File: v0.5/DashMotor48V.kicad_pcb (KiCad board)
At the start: 6 copper layers, 72 x 69.7 mm, 115 parts, among them CN3(OUT)1 XT30(2+2)PB-M.G.B, CN3(OUT)2 XT30(2+2)PB-M.G.B, J1 BM07B-SRSS-TB(LF)(SN), J2 BM07B-SRSS-TB(LF)(SN), J3 Conn_01x02_Pin, Q1 FDMT80080DC, Q2 FDMT80080DC, Q3 FDMT80080DC, Q4 FDMT80080DC, Q5 FDMT80080DC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

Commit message: finish first draft
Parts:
- removed TP2: +48V TestPoint, TestPoint:TestPoint_THTPad_D1.5mm_Drill0.7mm
- removed TP_GND1: GND TestPoint, TestPoint:TestPoint_THTPad_D1.5mm_Drill0.7mm
- R3: moved to B.Cu
- moved TP9 67.9 mm to (28.2, -0.72)
- moved TP8 67.4 mm to (27.6, -2.90)
- moved TP7 63.9 mm to (26.5, -4.92)
- moved TP10 63.3 mm to (25.6, -7.00)
- moved TP_GND2 59.5 mm to (-21.8, 13.5)
- moved TP12 50.9 mm to (6.80, -6.17)
- moved TP11 49.2 mm to (11.0, -32.3)
- moved TP13 44.8 mm to (8.82, -32.7)
- moved TP14 43.2 mm to (7.15, -31.2)
- moved TP4 30.4 mm to (-12.5, -22.2)
- moved TP1 27.5 mm to (-10.8, -9.68)
- moved TP5 26.1 mm to (7.80, -26.7)
- moved TP6 26.1 mm to (6.78, -28.6)
- moved R3 22.9 mm to (6.56, -14.1), turned to 180 degrees
- moved TP3 13.1 mm to (21.0, -19.9)
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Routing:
- net GND: track 19.4 -> 124.7 mm, vias 38 -> 101
- net /SPI-NSS-DRV: track 23.0 -> 65.1 mm
- net /SPI-SCK: track 22.3 -> 63.6 mm
- net +3.3V: track 61.5 -> 100.5 mm, vias 5 -> 11
- net /SPI-MISO: track 19.2 -> 56.8 mm
- net /SPI-MOSI: track 16.9 -> 51.5 mm
- net /SCK: track 46.6 -> 57.5 mm
- net Net-(VR1-FB): track 13.4 -> 23.9 mm
- net /CAN_RX: track 15.9 -> 26.2 mm, vias 0 -> 1
- net /MISO: track 44.3 -> 54.2 mm
- net /MOSI: track 44.0 -> 51.1 mm
- net +5V: track 25.1 -> 31.7 mm
- net /CAN_TX: track 19.9 -> 25.7 mm, vias 0 -> 1
- net /CS: track 24.0 -> 26.2 mm
- net Net-(U2-VCP): track 9.50 -> 7.86 mm
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- added copper zone on F.Cu, net +12V
- added copper zone on F.Cu, net +3.3V
- added copper zone on F.Cu, net /GHA
- added copper zone on F.Cu, net /GHB
- added copper zone on F.Cu, net /GHC
- added copper zone on F.Cu, net /GLA
- added copper zone on F.Cu, net /GLB
- added copper zone on F.Cu, net /GLC
- added copper zone on F.Cu, net GND
- added copper zone on F.Cu, net Net-(U2-VCP)
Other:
- board text removed: "3.3V"
- board text removed: "INDIC"

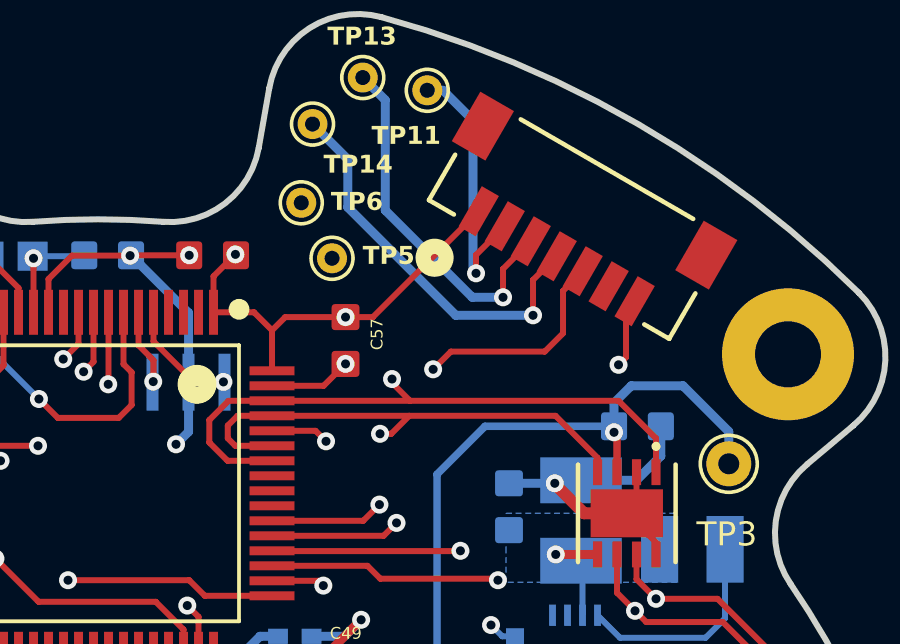
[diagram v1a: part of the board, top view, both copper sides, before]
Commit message: fix canrx tx pin place
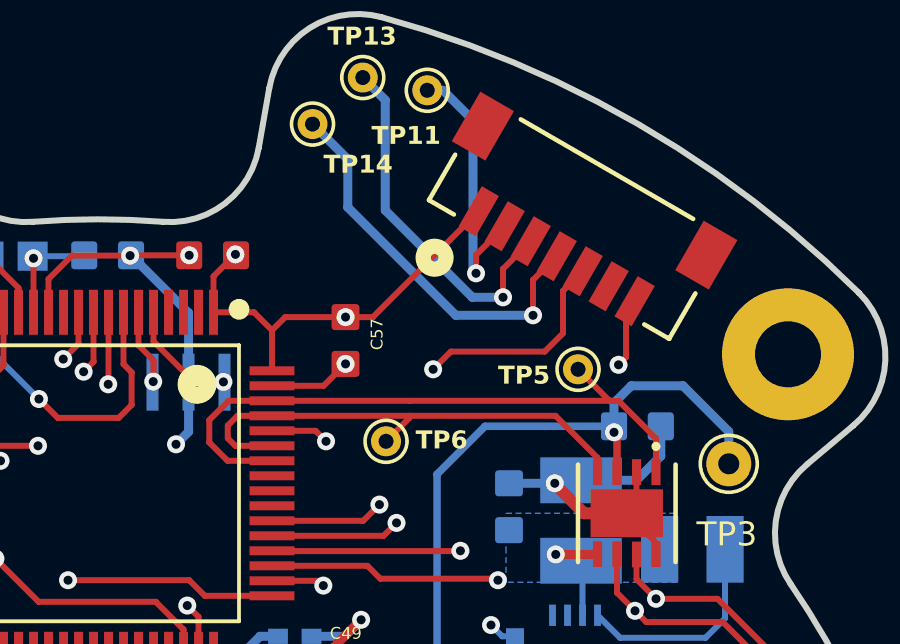
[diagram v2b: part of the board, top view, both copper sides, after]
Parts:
- moved TP5 9.00 mm to (16.0, -23.0)
- moved TP6 8.44 mm to (9.60, -20.6)
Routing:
- net /CAN_RX: track 26.2 -> 17.1 mm, vias 1 -> 0
- net /CAN_TX: track 25.7 -> 21.7 mm, vias 1 -> 0

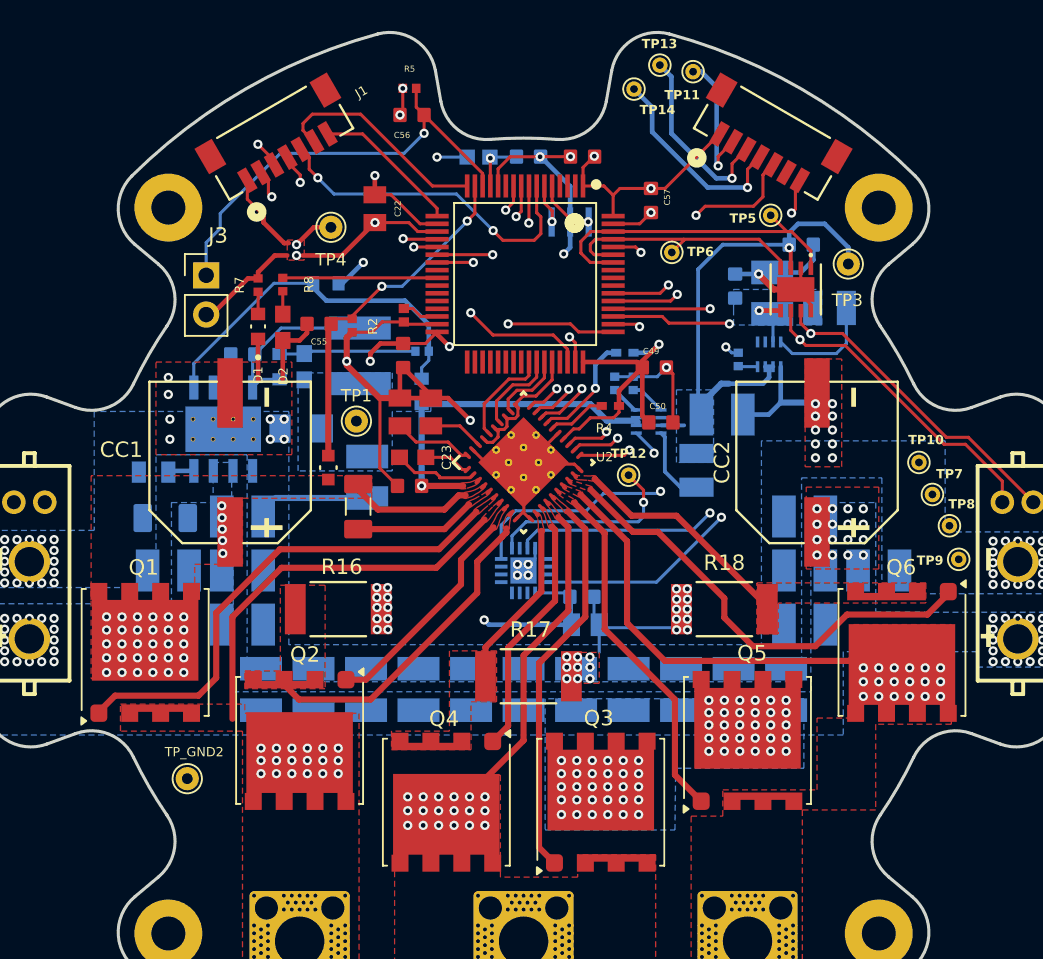
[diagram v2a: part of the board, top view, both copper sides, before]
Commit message: keep tuning few things
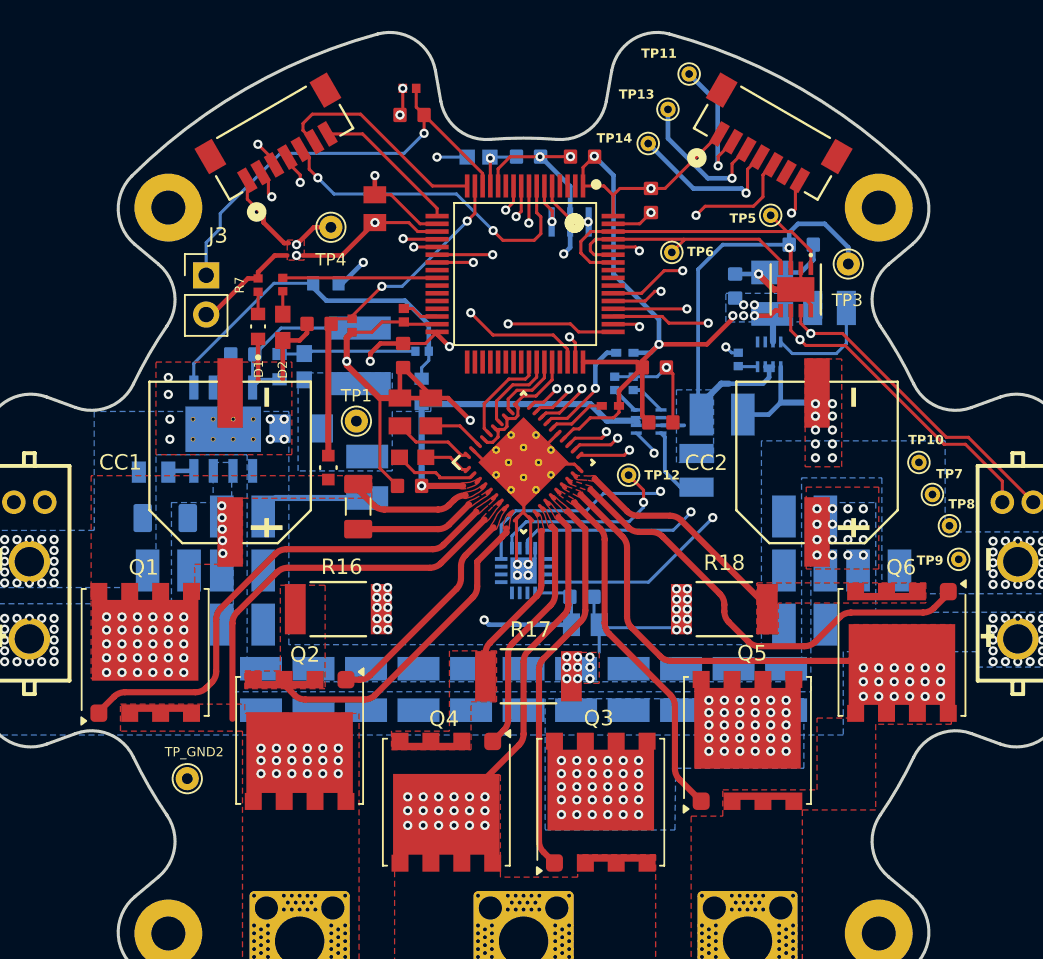
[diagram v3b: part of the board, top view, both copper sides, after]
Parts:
- moved TP14 3.64 mm to (8.07, -27.6)
- moved TP13 2.91 mm to (9.35, -29.9)
- moved TP11 0.30 mm to (10.7, -32.1)
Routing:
- net +3.3V: track 100.5 -> 130.3 mm, vias 11 -> 15
- net /SCK: track 57.5 -> 51.4 mm
- net GND: track 124.7 -> 130.5 mm
- net /MISO: track 54.2 -> 49.2 mm
- net /MOSI: track 51.1 -> 49.8 mm

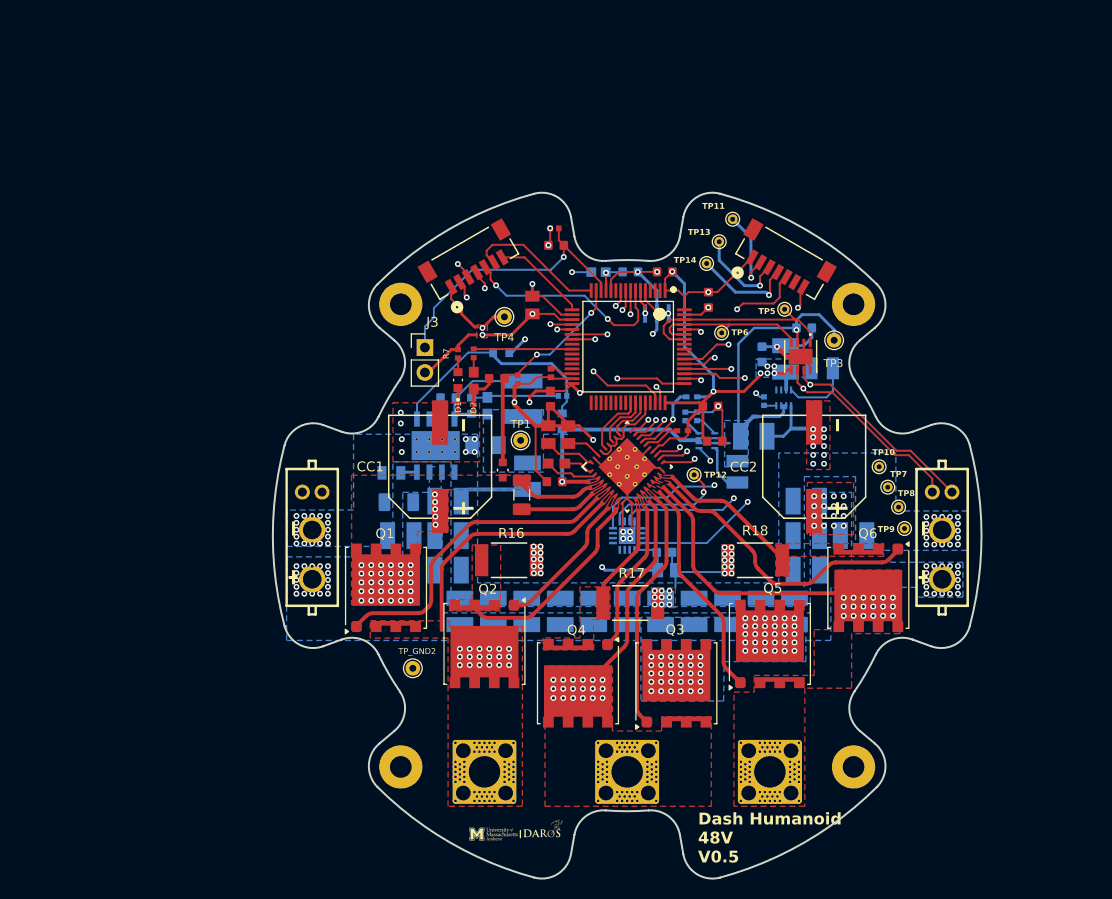
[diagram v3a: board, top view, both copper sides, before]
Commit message: adding more copper to the board
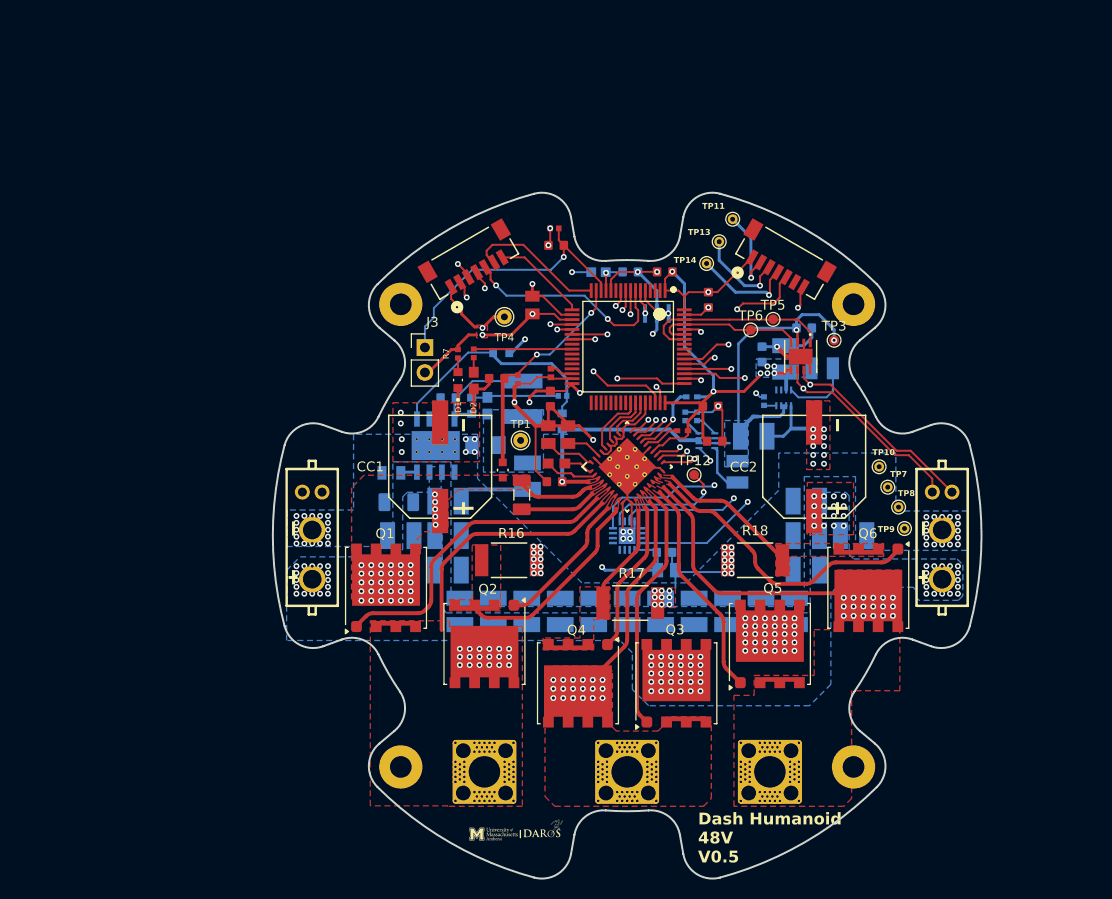
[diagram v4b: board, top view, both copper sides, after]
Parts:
- removed TP_GND2: GND TestPoint, TestPoint:TestPoint_THTPad_D1.5mm_Drill0.7mm
- TP12, TP5, TP6: footprint TestPoint:TestPoint_THTPad_D1.0mm_Drill0.5mm -> TestPoint:TestPoint_Pad_D1.0mm
- TP3: footprint TestPoint:TestPoint_THTPad_D1.5mm_Drill0.7mm -> TestPoint:TestPoint_Pad_D1.0mm
- moved TP6 2.97 mm to (12.6, -20.9)
- moved TP5 1.56 mm to (14.8, -22.0)
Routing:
- net /CAN_TX: track 21.7 -> 20.2 mm
- net /CAN_RX: track 17.1 -> 15.9 mm
- net +5V: vias 1 -> 2

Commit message: keep finishing it
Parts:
- removed TP1: +12V TestPoint, TestPoint:TestPoint_THTPad_D1.5mm_Drill0.7mm
- R14: moved to F.Cu
- TP10, TP7, TP8, TP9: footprint TestPoint:TestPoint_THTPad_D1.0mm_Drill0.5mm -> TestPoint:TestPoint_Pad_D1.0mm
- TP4: footprint TestPoint:TestPoint_THTPad_D1.5mm_Drill0.7mm -> TestPoint:TestPoint_Pad_D1.0mm
- moved TP8 43.9 mm to (-11.8, -22.2)
- moved TP9 43.9 mm to (-9.60, -23.0)
- moved TP10 39.6 mm to (-11.8, -20.0)
- moved TP7 38.7 mm to (-9.60, -18.9)
- moved R6 14.6 mm to (-27.1, -8.43)
- moved R14 4.52 mm to (-10.4, -14.8), turned to 0 degrees
- moved R2 3.08 mm to (-14.2, -15.7)
- moved C40 2.69 mm to (15.6, -10.1)
- moved C42 2.55 mm to (-6.60, -11.7)
- moved L1 2.45 mm to (-10.4, -11.4)
- moved C43 2.40 mm to (-14.1, -10.8)
- moved R9 2.40 mm to (-6.70, -9.20)
- moved C22 2.38 mm to (-10.6, -25.6), turned to 180 degrees
- moved TP4 2.33 mm to (-14.7, -22.9)
- moved L2 2.11 mm to (11.7, -8.55)
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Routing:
- net GND: track 130.5 -> 79.2 mm, vias 101 -> 98
- net /SPI-NSS-DRV: track 65.1 -> 27.3 mm
- net /SPI-SCK: track 63.6 -> 28.4 mm
- net /SPI-MOSI: track 51.5 -> 21.3 mm
- net /SPI-MISO: track 56.8 -> 29.2 mm
- net +3.3V: track 130.3 -> 113.3 mm, vias 15 -> 14
- net /VBAT: track 22.8 -> 31.7 mm, vias 2 -> 4
- net +12V: track 22.7 -> 19.7 mm
- net /CS: track 25.8 -> 22.8 mm
- net +5V: track 31.7 -> 29.0 mm
- net +48V: track 8.13 -> 10.4 mm
- net Net-(VR1-FB): track 23.9 -> 21.7 mm, vias 0 -> 1
- net Net-(U5-SW): track 5.06 -> 3.62 mm
- net /MOSI: track 49.8 -> 48.6 mm
- net /SCK: track 51.4 -> 50.3 mm
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- added copper zone on In3.Cu, net +3.3V
- added copper zone on In3.Cu, net +48V

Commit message: fine tune
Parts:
- C48, R14: moved to B.Cu
- moved R14 13.1 mm to (-23.0, -11.0), turned to 90 degrees
- moved C48 5.28 mm to (-2.75, -15.4), turned to 0 degrees
- moved C51 4.92 mm to (-11.1, -8.70), turned to 90 degrees
- moved R9 2.84 mm to (-4.40, -10.9)
- moved C49 1.81 mm to (9.85, -12.0)
- moved C50 1.36 mm to (9.85, -10.6)
- moved C20 1.30 mm to (-12.0, -4.00)
- moved C26 1.03 mm to (-8.28, -15.7)
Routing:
- net +3.3V: track 113.3 -> 76.7 mm, vias 14 -> 15
- net +12V: track 19.7 -> 8.29 mm
- net GND: track 79.2 -> 76.4 mm, vias 98 -> 114
- net Net-(VR1-FB): track 21.7 -> 23.5 mm, vias 1 -> 0
- net /PHASA: track 25.4 -> 26.8 mm, vias 18 -> 32
- net Net-(U2-VCP): track 7.81 -> 9.16 mm
- net +48V: track 10.4 -> 9.14 mm, vias 143 -> 150
- net /TCK: track 29.4 -> 28.2 mm
- net /MISO: track 48.3 -> 49.1 mm
- net /SPI-MISO: track 29.2 -> 28.5 mm
- net /CAN+: track 77.3 -> 76.7 mm
- net /PHASC: vias 18 -> 32
- net /PHASB: vias 18 -> 32
- added copper zone on B.Cu, net /PHASA
- added copper zone on In2.Cu, net /PHASA
- added copper zone on In3.Cu, net /PHASA
- added copper zone on B.Cu, net /PHASB
- added copper zone on In2.Cu, net /PHASB
- added copper zone on In3.Cu, net /PHASB
- added copper zone on B.Cu, net /PHASC
- added copper zone on In2.Cu, net /PHASC
- added copper zone on In3.Cu, net /PHASC
- added copper zone on In2.Cu, net GND
- added copper zone on In3.Cu, net GND

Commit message: doing fine touch for the routing, almost done
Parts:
- removed TP11: TP_MOSI, TestPoint:TestPoint_THTPad_D1.0mm_Drill0.5mm
- removed TP13: TP_MISO, TestPoint:TestPoint_THTPad_D1.0mm_Drill0.5mm
- removed TP14: TP_SCK, TestPoint:TestPoint_THTPad_D1.0mm_Drill0.5mm
- moved R3 5.40 mm to (1.33, -15.4), turned to 0 degrees
- moved C48 2.00 mm to (-0.91, -16.2), turned to 90 degrees
- moved R11 1.45 mm to (8.55, -12.2)
- moved R10 1.45 mm to (7.35, -12.2)
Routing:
- net +3.3V: track 76.7 -> 64.9 mm
- net /SCK: track 50.3 -> 42.6 mm
- net /MISO: track 49.1 -> 42.0 mm
- net /MOSI: track 48.9 -> 42.2 mm
- net GND: track 76.4 -> 71.5 mm, vias 114 -> 113
- net /SPI-MISO: track 28.5 -> 31.0 mm
- net +12V: track 8.29 -> 7.27 mm, vias 1 -> 4
- net +5V: track 29.0 -> 29.9 mm, vias 2 -> 3
- net Net-(U5-FB/VSET): track 2.33 -> 1.50 mm
- net /CAN_RX: track 15.9 -> 15.2 mm
- net /VMOT_TEMP: track 29.0 -> 28.5 mm
- net Net-(U5-MODE/S-CONF): track 1.93 -> 1.42 mm
- added copper zone on F.Cu, net +5V
